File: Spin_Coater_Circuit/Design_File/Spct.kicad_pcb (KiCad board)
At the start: 2 copper layers, 88 x 120 mm, 47 parts, among them J1 Conn_01x02_Pin, J2 Conn_01x03_Pin, J3 Conn_01x08_Pin, J4 Conn_01x02_Pin, J5 Conn_01x04_Pin, J6 Conn_01x02_Pin, J7 Conn_01x06_Pin, J8 Conn_01x02_Pin, J9 Conn_01x02_Pin, Q1 PNP, Q2 PNP, Q3 PNP, U1 NUCLEO-F401RE, U2 MCP4922-EP, U4 24LC512

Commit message: Change Ver1.1
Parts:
- removed Q1: PNP, Package_TO_SOT_THT:TO-92
- added D5: Zener_6V, Diode_THT:D_5W_P12.70mm_Horizontal, F.Cu at (62.1, 79.0)
- BZ1: value Buzzer -> IMT12D2001AP-Buzzer
- C2: footprint Capacitor_THT:C_Disc_D3.4mm_W2.1mm_P2.50mm -> Capacitor_THT:C_Disc_D4.3mm_W1.9mm_P5.00mm; moved to B.Cu
- C3: footprint Capacitor_THT:C_Disc_D3.4mm_W2.1mm_P2.50mm -> Capacitor_THT:C_Disc_D4.3mm_W1.9mm_P5.00mm
- D1: value Zener_12V -> Zener_6V; footprint Diode_THT:D_5W_P10.16mm_Horizontal -> Diode_THT:D_5W_P12.70mm_Horizontal; moved to F.Cu
- Q2, Q3: value PNP -> NPN; footprint Package_TO_SOT_THT:TO-92 -> Package_TO_SOT_THT:TO-92L_Inline_Wide_ECB
- R1: value 330 -> 100; footprint Resistor_THT:R_Axial_DIN0204_L3.6mm_D1.6mm_P5.08mm_Horizontal -> Resistor_THT:R_Axial_DIN0207_L6.3mm_D2.5mm_P10.16mm_Horizontal
- R10, R11, R12, R13, R14, R16, R17, R18, R2, R3, R4, R5, R6, R8, R9: footprint Resistor_THT:R_Axial_DIN0204_L3.6mm_D1.6mm_P5.08mm_Horizontal -> Resistor_THT:R_Axial_DIN0207_L6.3mm_D2.5mm_P10.16mm_Horizontal
- R7: value 10k -> 100; footprint Resistor_THT:R_Axial_DIN0204_L3.6mm_D1.6mm_P5.08mm_Horizontal -> Resistor_THT:R_Axial_DIN0207_L6.3mm_D2.5mm_P10.16mm_Horizontal
- U3: value ~ -> 367661
- moved R7 5.25 mm to (85.5, 134.8)
- moved R4 5.17 mm to (105.8, 144.1)
- moved D4 5.16 mm to (48.2, 135.6)
- moved R10 5.03 mm to (95.5, 135.0)
- moved D1 4.41 mm to (66.8, 66.3)
- moved R2 3.90 mm to (105.8, 121.2)
- moved R13 3.23 mm to (68.5, 59.5)
- moved R8 3.17 mm to (72.9, 59.5)
- moved R14 3.01 mm to (64.3, 59.4)
- moved R6 2.10 mm to (89.5, 124.6)
- moved U4 0.78 mm to (75.0, 85.6)
- moved R5 0.76 mm to (47.5, 119.7)
- moved C2 0.35 mm to (86.8, 142.7)
- turned Q2 to 180 degrees
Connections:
- D1 pad 2: +12V -> Net-(D1-A)
- Q2 pad 2: EMO -> Net-(Q2-C)
- Q2 pad 3: Net-(Q2-E) -> EMO
- Q3 pad 2: Lid_Sensor -> Net-(Q2-C)
- Q3 pad 3: Net-(Q2-E) -> Lid_Sensor
- R11 pad 1: Net-(J3-Pin_8) -> cRPM_METER
- R11 pad 2: +3V3 -> Net-(J3-Pin_8)
- R4 pad 1: cRPM_METER -> Phase_MON
- R5 pad 1: Net-(U3-Ready) -> READY_IN
- R7 pad 2: Net-(Q2-E) -> Net-(Q2-C)
- U1 pad CN10_35: unconnected-(U1B-PA2-PadCN10_35) -> Phase_MON
- U1 pad CN7_2: unconnected-(U1A-PC11-PadCN7_2) -> READY_IN
- U3 pad 10: Net-(U3-Ready) -> READY_IN
- U3 pad 13: Net-(Q2-E) -> Net-(Q2-C)
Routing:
- net Net-(Q2-C): track 0.00 -> 109.6 mm
- net READY_IN: track 0.00 -> 102.2 mm
- net Net-(Q2-E): track 101.0 -> 0.00 mm
- net +3V3: track 247.0 -> 172.9 mm
- net Phase_MON: track 0.00 -> 52.5 mm
- net cRPM_METER: track 105.1 -> 53.9 mm
- net Net-(U3-Ready): track 34.9 -> 0.00 mm
- net +12V: track 28.5 -> 39.9 mm
- net Lid_Sensor: track 69.6 -> 80.5 mm
- net Net-(J3-Pin_8): track 43.3 -> 33.7 mm
- net EMO: track 68.6 -> 77.2 mm
- net pBuzzer: track 16.1 -> 9.98 mm
- net Net-(D1-A): track 0.00 -> 5.54 mm
- net SW_LED: track 74.8 -> 79.9 mm
- net aSPEED: track 39.0 -> 44.1 mm
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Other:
- board text added: "Spin_Coater V1.1 23.05.25"
- board text removed: "Spin_Coater V1.0 23.03.19"

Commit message: Circuit version 1.2
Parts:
- removed D1, D5: Zener_6V, Diode_THT:D_5W_P12.70mm_Horizontal
- added U5: SZH-PWSD-026, Symbol:DCDC_SZH-PWSD-026, F.Cu at (64.5, 77.3)
- moved U2 2.24 mm to (76.1, 107.5)
- moved U4 1.31 mm to (76.3, 85.7)
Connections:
- C2 pad 1: Net-(J3-Pin_5) -> +24V
- J3 pad 5: Net-(J3-Pin_5) -> +24V
- Q2 pad 1: GND -> Net-(Q2-D)
- Q2 pad 2: Net-(Q2-C) -> EMO
- Q2 pad 3: EMO -> GND
- Q3 pad 1: GND -> Net-(Q2-D)
- Q3 pad 2: Net-(Q2-C) -> Lid_Sensor
- Q3 pad 3: Lid_Sensor -> GND
- R7 pad 2: Net-(Q2-C) -> Net-(Q2-D)
- U3 pad 13: Net-(Q2-C) -> Net-(Q2-D)
- U3 pad 6: Net-(J3-Pin_5) -> +24V
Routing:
- net Net-(Q2-C): track 109.6 -> 0.00 mm
- net Net-(Q2-D): track 0.00 -> 108.6 mm
- net +24V: track 192.5 -> 222.8 mm
- net GND: track 0.81 -> 17.1 mm, vias 184 -> 161
- net Net-(J3-Pin_5): track 9.10 -> 0.00 mm
- net +12V: track 39.9 -> 32.1 mm
- net EMO: track 77.2 -> 82.8 mm
- net Net-(D1-A): track 5.54 -> 0.00 mm
- net +3V3: track 172.9 -> 176.9 mm
- net ADC_CS: track 66.9 -> 63.6 mm
- net ADC_UPDATE: track 33.2 -> 31.2 mm
- net TEMP: track 102.0 -> 100.0 mm
- net SCK: track 48.0 -> 46.0 mm
- net SDA: track 31.0 -> 29.8 mm
- net WP: track 41.4 -> 40.1 mm
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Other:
- board text added: "Spin_Coater V1.2 23.07.19"
- board text removed: "Spin_Coater V1.1 23.05.25"

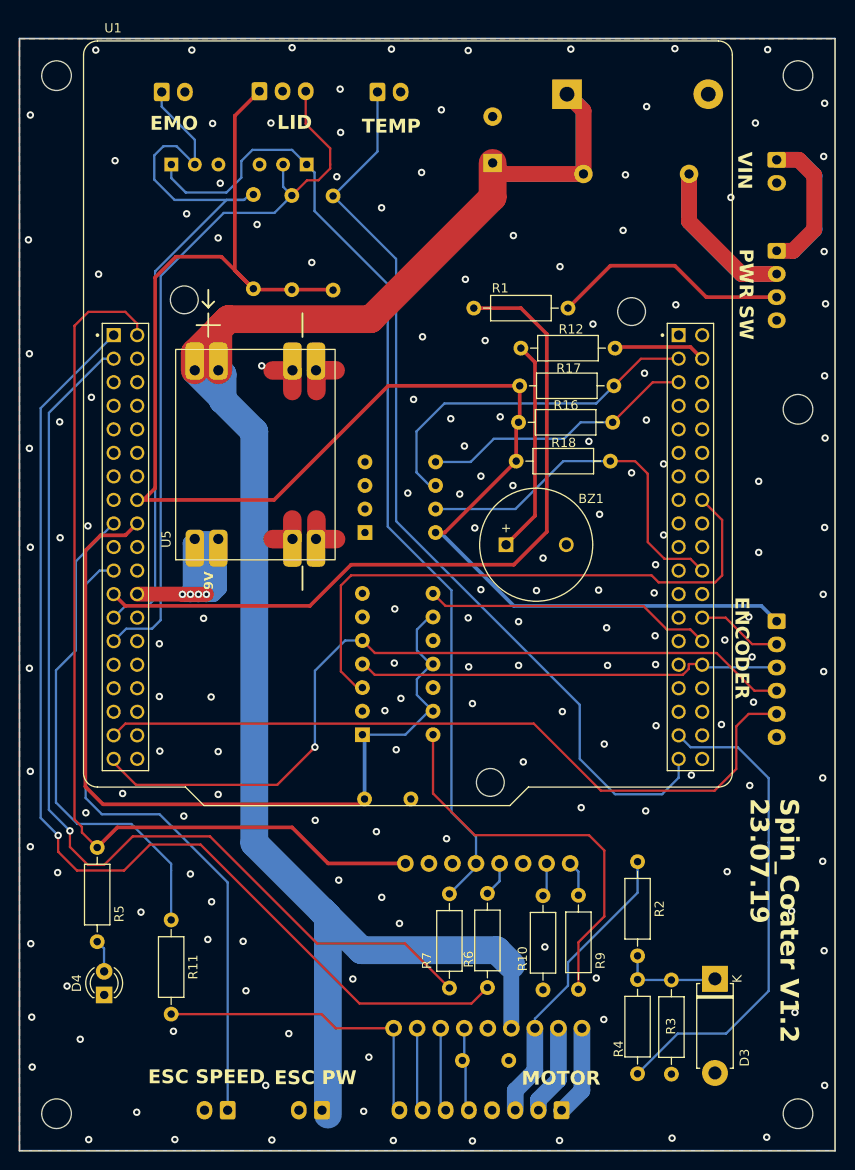
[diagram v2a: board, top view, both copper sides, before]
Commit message: Spin coater ver1.3
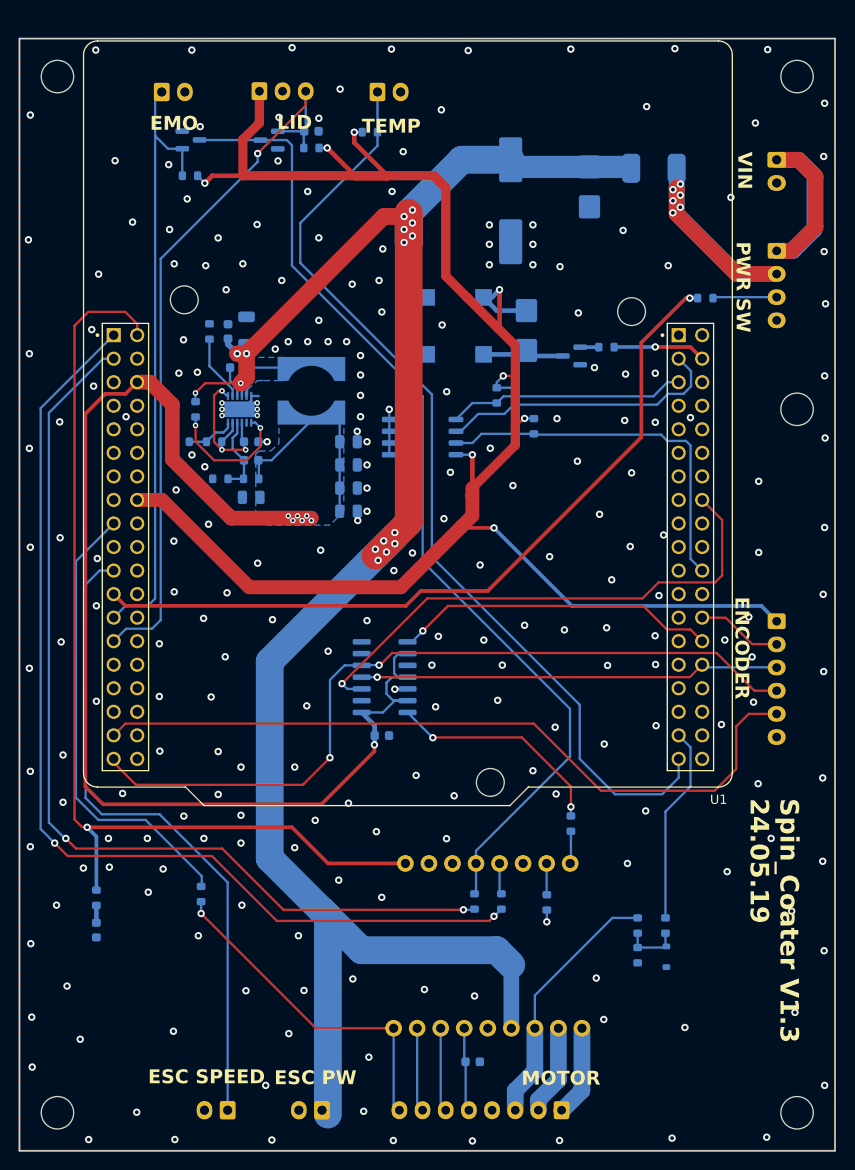
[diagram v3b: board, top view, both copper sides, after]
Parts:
- removed BZ1: IMT12D2001AP-Buzzer, Buzzer_Beeper:MagneticBuzzer_ProSignal_ABT-410-RC
- removed U5: SZH-PWSD-026, Symbol:DCDC_SZH-PWSD-026
- added C10: 10uF/10V, Capacitor_SMD:C_0805_2012Metric, B.Cu at (64.1, 81.9)
- added C11: 10uF/10V, Capacitor_SMD:C_0805_2012Metric, B.Cu at (74.6, 83.4)
- added C12: 100nF/50V, Capacitor_SMD:C_0603_1608Metric, B.Cu at (64.1, 83.9)
- added C13: 22uF/10V, Capacitor_SMD:C_0805_2012Metric, B.Cu at (74.6, 80.9)
- added C14: 22uF/10V, Capacitor_SMD:C_0805_2012Metric, B.Cu at (74.6, 78.4)
- added C15: 10uF/10V, Capacitor_SMD:C_0805_2012Metric, B.Cu at (74.6, 75.9)
- added C4: 100nF/50V, Capacitor_SMD:C_0603_1608Metric, B.Cu at (70.6, 42.4)
- added C5: 4.7F/50V, Capacitor_SMD:C_1206_3216Metric, B.Cu at (63.6, 63.9)
- added C6: 100nF/50V, Capacitor_SMD:C_0603_1608Metric, B.Cu at (61.6, 64.0)
- added C7: 100nF/50V, Capacitor_SMD:C_0603_1608Metric, B.Cu at (62.6, 67.9)
- added C8: 1uF/10V, Capacitor_SMD:C_0603_1608Metric, B.Cu at (64.1, 75.9)
- added C9: 27pF/10V, Capacitor_SMD:C_0603_1608Metric, B.Cu at (64.1, 77.9)
- added D1: B360B-13-F, Diode_SMD:D_SMB, B.Cu at (93.8, 63.9)
- added L1: 22uH, Custom_Library:L_Bourns_SRR6028, B.Cu at (70.6, 70.4)
- added LS1: CMT-7525-80-SMT-TR, Custom_Library:XDCR_CMT-7525-80-SMT-TR, B.Cu at (86.1, 63.4)
- added Q1: 2N7002, Package_TO_SOT_SMD:SOT-23, B.Cu at (98.6, 66.6)
- added R15: 10k, Resistor_SMD:R_0603_1608Metric, B.Cu at (60.7, 79.9)
- added R19: 75k, Resistor_SMD:R_0603_1608Metric, B.Cu at (64.1, 79.9)
- added R20: 75k, Resistor_SMD:R_0603_1608Metric, B.Cu at (58.1, 72.4)
- added R21: 0, Resistor_SMD:R_0603_1608Metric, B.Cu at (60.1, 75.9)
- added R22: N.C, Resistor_SMD:R_0603_1608Metric, B.Cu at (56.6, 75.9)
- added R23: 75k, Resistor_SMD:R_0603_1608Metric, B.Cu at (59.6, 64.0)
- added U6: ISL85410FRZ, Custom_Library:SON50P300X300X100-13N_270X200_, B.Cu at (62.8, 72.4)
- C1: value 330uF / 50V -> 330uF/50V; footprint Capacitor_THT:CP_Radial_D10.0mm_P5.00mm -> Custom_Library:CP_Elec_12.5x12.5
- C2, C3: value 100nF -> 100nF/50V; footprint Capacitor_THT:C_Disc_D4.3mm_W1.9mm_P5.00mm -> Capacitor_SMD:C_0603_1608Metric
- D2: value 1N5401 -> B360B-13-F; footprint Diode_THT:D_DO-201AD_P15.24mm_Horizontal -> Diode_SMD:D_SMB
- D3: value Zener_3.3V -> MM3Z3V3T1G; footprint Diode_THT:D_5W_P10.16mm_Horizontal -> Custom_Library:D_SOD-323-2; moved to B.Cu
- D4: value LED -> 150060BS55040; footprint LED_THT:LED_D3.0mm -> LED_SMD:LED_0603_1608Metric; moved to B.Cu
- F1: value Fuse_3A -> 0679H5000-01; footprint Fuse:Fuse_Littelfuse-LVR100 -> Custom_Library:Fuse_2410_6225_Metric
- J1, J4, J6, J8, J9: value Conn_01x02_Pin -> EH_B2B-EH-A
- J2: value Conn_01x03_Pin -> EH_B3B-EH-A
- J3: value Conn_01x08_Pin -> EH_B8B-EH-A
- J5: value Conn_01x04_Pin -> EH_B4B-EH-A
- J7: value Conn_01x06_Pin -> EH_B6B-EH-A
- Q2, Q3: value NPN -> 2N7002; footprint Package_TO_SOT_THT:TO-92L_Inline_Wide_ECB -> Package_TO_SOT_SMD:SOT-23
- R1, R10, R11, R12, R16, R17, R18, R2, R3, R4, R5, R6, R7, R9: footprint Resistor_THT:R_Axial_DIN0207_L6.3mm_D2.5mm_P10.16mm_Horizontal -> Resistor_SMD:R_0603_1608Metric; moved to B.Cu
- R13, R14, R8: footprint Resistor_THT:R_Axial_DIN0207_L6.3mm_D2.5mm_P10.16mm_Horizontal -> Resistor_SMD:R_0603_1608Metric
- REF** (x5): value MountingHole_3.2mm_M3 -> MountingHole_3.5mm; footprint MountingHole:MountingHole_3.2mm_M3 -> MountingHole:MountingHole_3.5mm
- U1: value NUCLEO-F401RE -> NUCLEO-F411RE
- U2: value MCP4922-EP -> MCP4922-E/SL; footprint Package_DIP:DIP-14_W7.62mm_Socket -> Package_SO:SOIC-14_3.9x8.7mm_P1.27mm
- U4: value 24LC512 -> 24LC512T-I/SN; footprint Package_DIP:DIP-8_W7.62mm_Socket -> Package_SO:SOIC-8_5.275x5.275mm_P1.27mm
- moved R8 17.5 mm to (76.9, 42.5), turned to 0 degrees
- moved R4 16.3 mm to (108.8, 128.1), turned to -90 degrees
- moved R13 15.4 mm to (70.6, 44.2), turned to 180 degrees
- moved R1 14.9 mm to (113.1, 60.4)
- moved R14 14.0 mm to (57.5, 47.2), turned to 180 degrees
- moved U4 12.0 mm to (82.6, 75.4)
- moved D2 10.3 mm to (100.6, 48.4), turned to -90 degrees
- moved R7 9.72 mm to (88.2, 125.5)
- moved R10 9.45 mm to (96.0, 125.6)
- moved R12 9.24 mm to (102.4, 65.7)
- moved F1 8.17 mm to (108.1, 46.4)
- moved R9 7.77 mm to (98.6, 117.1), turned to 90 degrees
- moved C3 7.09 mm to (78.2, 107.6)
- moved D4 7.05 mm to (47.4, 128.6)
- moved R2 6.89 mm to (105.8, 128.1)
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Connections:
- C2 pad 1: +24V -> Net-(J3-Pin_5)
- C3 pad 1: +5V -> +E5V
- J3 pad 5: +24V -> Net-(J3-Pin_5)
- Q2 pad 1: Net-(Q2-D) -> EMO
- Q2 pad 2: EMO -> GND
- Q2 pad 3: GND -> Net-(Q2-D)
- Q3 pad 1: Net-(Q2-D) -> Lid_Sensor
- Q3 pad 2: Lid_Sensor -> GND
- Q3 pad 3: GND -> Net-(Q2-D)
- U1 pad CN7_18: +5V -> unconnected-(U1A-+5V_S1-PadCN7_18)
- U1 pad CN7_6: unconnected-(U1A-E5V-PadCN7_6) -> +E5V
- U2 pad 1: +5V -> +E5V
- U2 pad 11: +5V -> +E5V
- U2 pad 13: +5V -> +E5V
- U2 pad 9: +5V -> +E5V
- U3 pad 6: +24V -> Net-(J3-Pin_5)
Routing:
- net +E5V: track 0.00 -> 150.9 mm, vias 0 -> 7
- net +5V: track 93.1 -> 0.00 mm
- net +12V: track 32.1 -> 0.00 mm, vias 4 -> 0
- net Phase_MON: track 52.5 -> 21.3 mm
- net +3V3: track 176.9 -> 200.6 mm, vias 0 -> 8
- net Net-(Q1-G): track 23.1 -> 2.02 mm
- net aSPEED: track 43.5 -> 24.1 mm, vias 0 -> 2
- net Net-(J5-Pin_3): track 25.8 -> 6.47 mm
- net Net-(U6-COMP): track 0.00 -> 17.3 mm, vias 0 -> 3
- net EMO: track 82.8 -> 66.7 mm
- net Net-(U6-EN): track 0.00 -> 14.4 mm, vias 0 -> 2
- net +24V: track 222.8 -> 212.6 mm, vias 0 -> 16
- net Net-(J3-Pin_5): track 0.00 -> 9.10 mm
- net Net-(D1-A): track 0.00 -> 8.97 mm
- net Net-(U6-FB): track 0.00 -> 8.48 mm
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- added copper zone on B.Cu, net +E5V
- added copper zone on B.Cu, net Net-(U6-PHASE)
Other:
- board text added: "Spin_Coater V1.3 24.05.19"
- board text removed: "Spin_Coater V1.2 23.07.19"
